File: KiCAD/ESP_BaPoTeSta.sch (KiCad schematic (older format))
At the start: 22 parts, among them P1 Progr, P2 Battery, P3 Power, P4 Upload, P5 Config, U1 MCP1700-330, U2 ESP-12, U3 DS18B20, U4 DHT22

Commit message: ENH: replace 4k7 resistor by 2 10k
so I don't have to buy 4k7 resistors
Enlarge ground plane beneath ESP
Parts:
- added R11: 10k, Resistors_SMD:R_1206_HandSoldering, symbol R
- R7: value 4k7 -> 10k
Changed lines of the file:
@@
 $EndComp
 $Comp
-L VCC #PWR01
+L VCC #PWR4
 U 1 1 566291DB
 P 5850 2100
-F 0 "#PWR01" H 5850 1950 50  0001 C CNN
+F 0 "#PWR4" H 5850 1950 50  0001 C CNN
 F 1 "VCC" H 5850 2250 50  0000 C CNN
 F 2 "" H 5850 2100 50  0000 C CNN
@@
 $EndComp
 $Comp
-L GND #PWR02
+L GND #PWR5
 U 1 1 56629270
 P 5850 3950
-F 0 "#PWR02" H 5850 3700 50  0001 C CNN
+F 0 "#PWR5" H 5850 3700 50  0001 C CNN
 F 1 "GND" H 5850 3800 50  0000 C CNN
 F 2 "" H 5850 3950 50  0000 C CNN
@@
 	6950 2800 6950 1650
 $Comp
-L GND #PWR03
+L GND #PWR6
 U 1 1 5662AF46
 P 7050 1750
-F 0 "#PWR03" H 7050 1500 50  0001 C CNN
+F 0 "#PWR6" H 7050 1500 50  0001 C CNN
 F 1 "GND" H 7050 1600 50  0000 C CNN
 F 2 "" H 7050 1750 50  0000 C CNN
@@
 	4600 2500 2150 2500
 $Comp
-L PWR_FLAG #FLG04
+L PWR_FLAG #FLG1
 U 1 1 5662B03F
 P 1550 2100
-F 0 "#FLG04" H 1550 2195 50  0001 C CNN
+F 0 "#FLG1" H 1550 2195 50  0001 C CNN
 F 1 "PWR_FLAG" H 1550 2280 50  0000 C CNN
 F 2 "" H 1550 2100 50  0000 C CNN
@@
 $EndComp
 $Comp
-L PWR_FLAG #FLG05
+L PWR_FLAG #FLG2
 U 1 1 5662B14A
 P 1550 3000
-F 0 "#FLG05" H 1550 3095 50  0001 C CNN
+F 0 "#FLG2" H 1550 3095 50  0001 C CNN
 F 1 "PWR_FLAG" H 1550 3180 50  0000 C CNN
 F 2 "" H 1550 3000 50  0000 C CNN
@@
 P 4900 1100
 F 0 "R7" V 4980 1100 50  0000 C CNN
-F 1 "4k7" V 4900 1100 50  0000 C CNN
+F 1 "10k" V 4900 1100 50  0000 C CNN
 F 2 "Resistors_SMD:R_1206_HandSoldering" V 4830 1100 50  0001 C CNN
 F 3 "" H 4900 1100 50  0000 C CNN
@@
 $EndComp
 Wire Wire Line
-	4900 1250 5050 1250
+	4750 1250 5050 1250
 $Comp
 L CONN_01X02 P2
@@
 	1550 2600 1550 3000
 $Comp
-L +BATT #PWR06
+L +BATT #PWR1
 U 1 1 5662D0E0
 P 1550 2100
-F 0 "#PWR06" H 1550 1950 50  0001 C CNN
+F 0 "#PWR1" H 1550 1950 50  0001 C CNN
 F 1 "+BATT" H 1550 2240 50  0000 C CNN
 F 2 "" H 1550 2100 50  0000 C CNN
@@
 PwrSens
 Wire Wire Line
-	4900 950  5050 950
+	4750 950  5050 950
 Wire Wire Line
 	5050 950  5050 1150
@@
 	3000 3900 7600 3900
 $Comp
-L GND #PWR07
+L GND #PWR3
 U 1 1 568F994B
 P 5050 1550
-F 0 "#PWR07" H 5050 1300 50  0001 C CNN
+F 0 "#PWR3" H 5050 1300 50  0001 C CNN
 F 1 "GND" H 5050 1400 50  0000 C CNN
 F 2 "" H 5050 1550 50  0000 C CNN
@@
 	5050 1550 5050 1350
 $Comp
-L GND #PWR08
+L GND #PWR2
 U 1 1 568F99FF
 P 4100 1550
-F 0 "#PWR08" H 4100 1300 50  0001 C CNN
+F 0 "#PWR2" H 4100 1300 50  0001 C CNN
 F 1 "GND" H 4100 1400 50  0000 C CNN
 F 2 "" H 4100 1550 50  0000 C CNN
@@
 Connection ~ 3800 3900
 Connection ~ 3800 2100
+$Comp
+L R R11
+U 1 1 5692C067
+P 4750 1100
+F 0 "R11" V 4830 1100 50  0000 C CNN
+F 1 "10k" V 4750 1100 50  0000 C CNN
+F 2 "Resistors_SMD:R_1206_HandSoldering" V 4680 1100 50  0001 C CNN
+F 3 "" H 4750 1100 50  0000 C CNN
+	1    4750 1100
+	1    0    0    -1
+$EndComp
+Connection ~ 4900 1250
+Connection ~ 4900 950
 $EndSCHEMATC

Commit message: ENH: improve battery measurement accuracy
use 56k instead of 68k resistor
This will work up to 6.6V -- more than enough, as max
rated input voltage of the MCP1700 is only 6V
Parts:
- R1: value 68k -> 56k
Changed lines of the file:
@@
 $EndComp
 $Comp
-L VCC #PWR4
+L VCC #PWR01
 U 1 1 566291DB
 P 5850 2100
-F 0 "#PWR4" H 5850 1950 50  0001 C CNN
+F 0 "#PWR01" H 5850 1950 50  0001 C CNN
 F 1 "VCC" H 5850 2250 50  0000 C CNN
 F 2 "" H 5850 2100 50  0000 C CNN
@@
 $EndComp
 $Comp
-L GND #PWR5
+L GND #PWR02
 U 1 1 56629270
 P 5850 3950
-F 0 "#PWR5" H 5850 3700 50  0001 C CNN
+F 0 "#PWR02" H 5850 3700 50  0001 C CNN
 F 1 "GND" H 5850 3800 50  0000 C CNN
 F 2 "" H 5850 3950 50  0000 C CNN
@@
 P 2150 2250
 F 0 "R1" V 2230 2250 50  0000 C CNN
-F 1 "68k" V 2150 2250 50  0000 C CNN
+F 1 "56k" V 2150 2250 50  0000 C CNN
 F 2 "Resistors_SMD:R_1206_HandSoldering" V 2080 2250 50  0001 C CNN
 F 3 "" H 2150 2250 50  0000 C CNN
@@
 	6950 2800 6950 1650
 $Comp
-L GND #PWR6
+L GND #PWR03
 U 1 1 5662AF46
 P 7050 1750
-F 0 "#PWR6" H 7050 1500 50  0001 C CNN
+F 0 "#PWR03" H 7050 1500 50  0001 C CNN
 F 1 "GND" H 7050 1600 50  0000 C CNN
 F 2 "" H 7050 1750 50  0000 C CNN
@@
 	4600 2500 2150 2500
 $Comp
-L PWR_FLAG #FLG1
+L PWR_FLAG #FLG04
 U 1 1 5662B03F
 P 1550 2100
-F 0 "#FLG1" H 1550 2195 50  0001 C CNN
+F 0 "#FLG04" H 1550 2195 50  0001 C CNN
 F 1 "PWR_FLAG" H 1550 2280 50  0000 C CNN
 F 2 "" H 1550 2100 50  0000 C CNN
@@
 $EndComp
 $Comp
-L PWR_FLAG #FLG2
+L PWR_FLAG #FLG05
 U 1 1 5662B14A
 P 1550 3000
-F 0 "#FLG2" H 1550 3095 50  0001 C CNN
+F 0 "#FLG05" H 1550 3095 50  0001 C CNN
 F 1 "PWR_FLAG" H 1550 3180 50  0000 C CNN
 F 2 "" H 1550 3000 50  0000 C CNN
@@
 	1550 2600 1550 3000
 $Comp
-L +BATT #PWR1
+L +BATT #PWR06
 U 1 1 5662D0E0
 P 1550 2100
-F 0 "#PWR1" H 1550 1950 50  0001 C CNN
+F 0 "#PWR06" H 1550 1950 50  0001 C CNN
 F 1 "+BATT" H 1550 2240 50  0000 C CNN
 F 2 "" H 1550 2100 50  0000 C CNN
@@
 	3000 3900 7600 3900
 $Comp
-L GND #PWR3
+L GND #PWR07
 U 1 1 568F994B
 P 5050 1550
-F 0 "#PWR3" H 5050 1300 50  0001 C CNN
+F 0 "#PWR07" H 5050 1300 50  0001 C CNN
 F 1 "GND" H 5050 1400 50  0000 C CNN
 F 2 "" H 5050 1550 50  0000 C CNN
@@
 	5050 1550 5050 1350
 $Comp
-L GND #PWR2
+L GND #PWR08
 U 1 1 568F99FF
 P 4100 1550
-F 0 "#PWR2" H 4100 1300 50  0001 C CNN
+F 0 "#PWR08" H 4100 1300 50  0001 C CNN
 F 1 "GND" H 4100 1400 50  0000 C CNN
 F 2 "" H 4100 1550 50  0000 C CNN

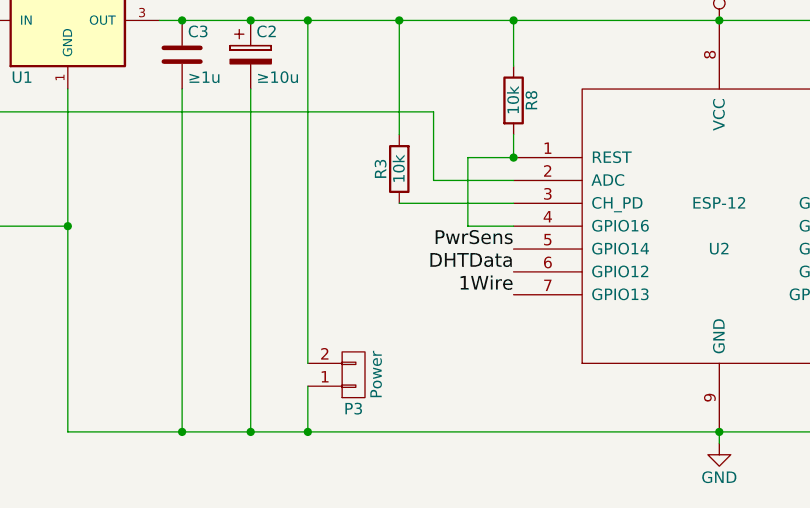
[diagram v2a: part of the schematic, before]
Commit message: ENH: [pcb] add SMD jumpers for data lines
makes it easier to re-use unused lines as GPIO
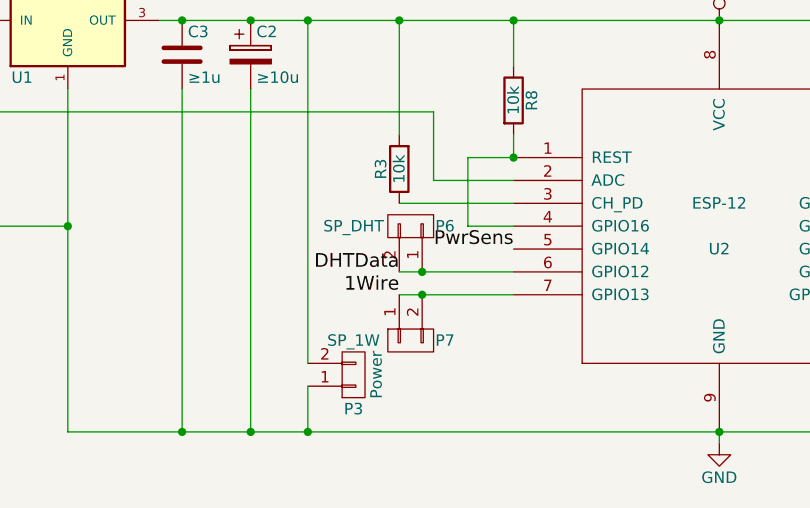
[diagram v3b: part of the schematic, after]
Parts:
- added P6: SP_DHT, open-project:S_JUMPER_2, symbol CONN_01X02
- added P7: SP_1W, open-project:S_JUMPER_2, symbol CONN_01X02
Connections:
- wire segments 48 -> 50
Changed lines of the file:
@@
 LIBS:maxim
 LIBS:sensors
+LIBS:open-project
 LIBS:ESP_BaPoTeSta-cache
 EELAYER 25 0
@@
 	1    0    0    -1
 $EndComp
-Text Label 4950 3300 2    60   ~ 0
+Text Label 4450 3300 2    60   ~ 0
 1Wire
 Text Label 4950 1250 3    60   ~ 0
@@
 	-1   0    0    -1
 $EndComp
-Text Label 4950 3200 2    60   ~ 0
+Text Label 4450 3200 2    60   ~ 0
 DHTData
 Text Label 3650 1250 3    60   ~ 0
@@
 Connection ~ 4900 1250
 Connection ~ 4900 950
+$Comp
+L CONN_01X02 P6
+U 1 1 569544C5
+P 4500 3000
+F 0 "P6" V 4500 3150 50  0000 C CNN
+F 1 "SP_DHT" V 4500 2750 50  0000 C CNN
+F 2 "open-project:S_JUMPER_2" H 4500 3000 50  0001 C CNN
+F 3 "" H 4500 3000 50  0000 C CNN
+	1    4500 3000
+	0    1    -1   0
+$EndComp
+$Comp
+L CONN_01X02 P7
+U 1 1 56954571
+P 4500 3500
+F 0 "P7" V 4500 3350 50  0000 C CNN
+F 1 "SP_1W" V 4500 3750 50  0000 C CNN
+F 2 "open-project:S_JUMPER_2" H 4500 3500 50  0001 C CNN
+F 3 "" H 4500 3500 50  0000 C CNN
+	1    4500 3500
+	0    -1   1    0
+$EndComp
+Wire Wire Line
+	4450 3200 4950 3200
+Wire Wire Line
+	4450 3300 4950 3300
+Connection ~ 4550 3200
+Connection ~ 4550 3300
 $EndSCHEMATC

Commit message: ENH: [pcb] minor silkscreen fixes
also, finish f41bc1a
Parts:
- C2: footprint Capacitors_ThroughHole:C_Radial_D5_L11_P2 -> Capacitors_ThroughHole:C_Radial_D5_L11_P2.5
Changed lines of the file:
@@
 F 0 "C2" H 3825 2350 50  0000 L CNN
 F 1 "≥10u" H 3825 2150 50  0000 L CNN
-F 2 "Capacitors_ThroughHole:C_Radial_D5_L11_P2" H 3838 2100 50  0001 C CNN
+F 2 "Capacitors_ThroughHole:C_Radial_D5_L11_P2.5" H 3838 2100 50  0001 C CNN
 F 3 "" H 3800 2250 50  0000 C CNN
 	1    3800 2250

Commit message: ENH: started work on new board layout
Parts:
- removed P6: SP_DHT, open-project:S_JUMPER_2, symbol CONN_01X02
- removed P7: SP_1W, open-project:S_JUMPER_2, symbol CONN_01X02
- removed R10, R11, R7: 10k, Resistors_SMD:R_1206_HandSoldering, symbol R
- removed U2: ESP-12, ESP8266:ESP-12, symbol ESP-12
- removed U3: DS18B20, TO_SOT_Packages_THT:TO-92_Inline_Wide, symbol DS18B20
- removed U4: DHT22, Pin_Headers:Pin_Header_Straight_1x04, symbol DHT11
- added P10, P11, P12: CONN_01X04, symbol CONN_01X04
- added P13, P14, P15: CONN_01X03, symbol CONN_01X03
- added U2: ESP-12E, symbol ESP-12E
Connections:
- net labels added: BattFET, SCL, SDA
- wire segments 50 -> 71
- no-connect marks 1 -> 3
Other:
- moved on the sheet: R6

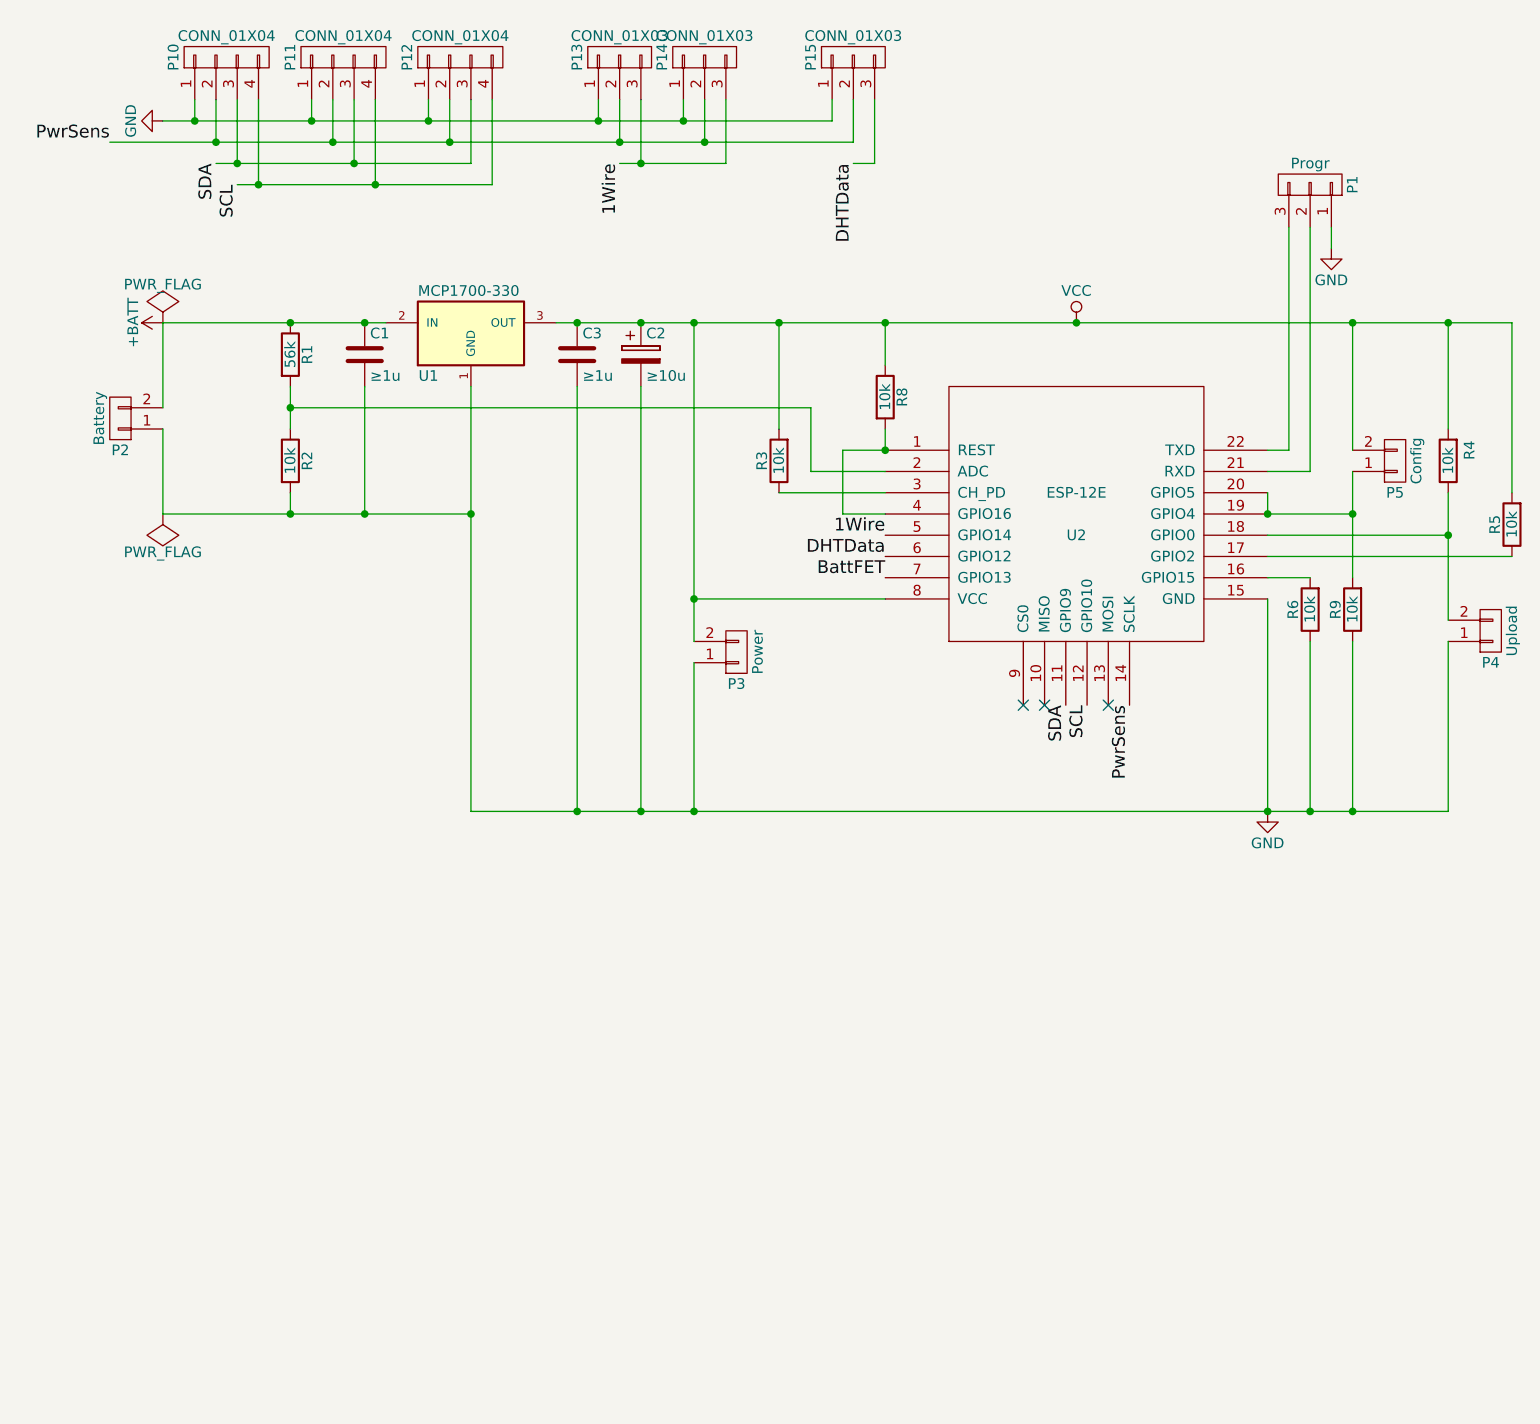
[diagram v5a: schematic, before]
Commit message: ENH: Redesigned schematic
now with 4 I2C, 2 1Wire and 1 DHT port.
Also added MOSFET for battery measurement,
and power-saving Schottky for GPIO16 -- thanks Malte!
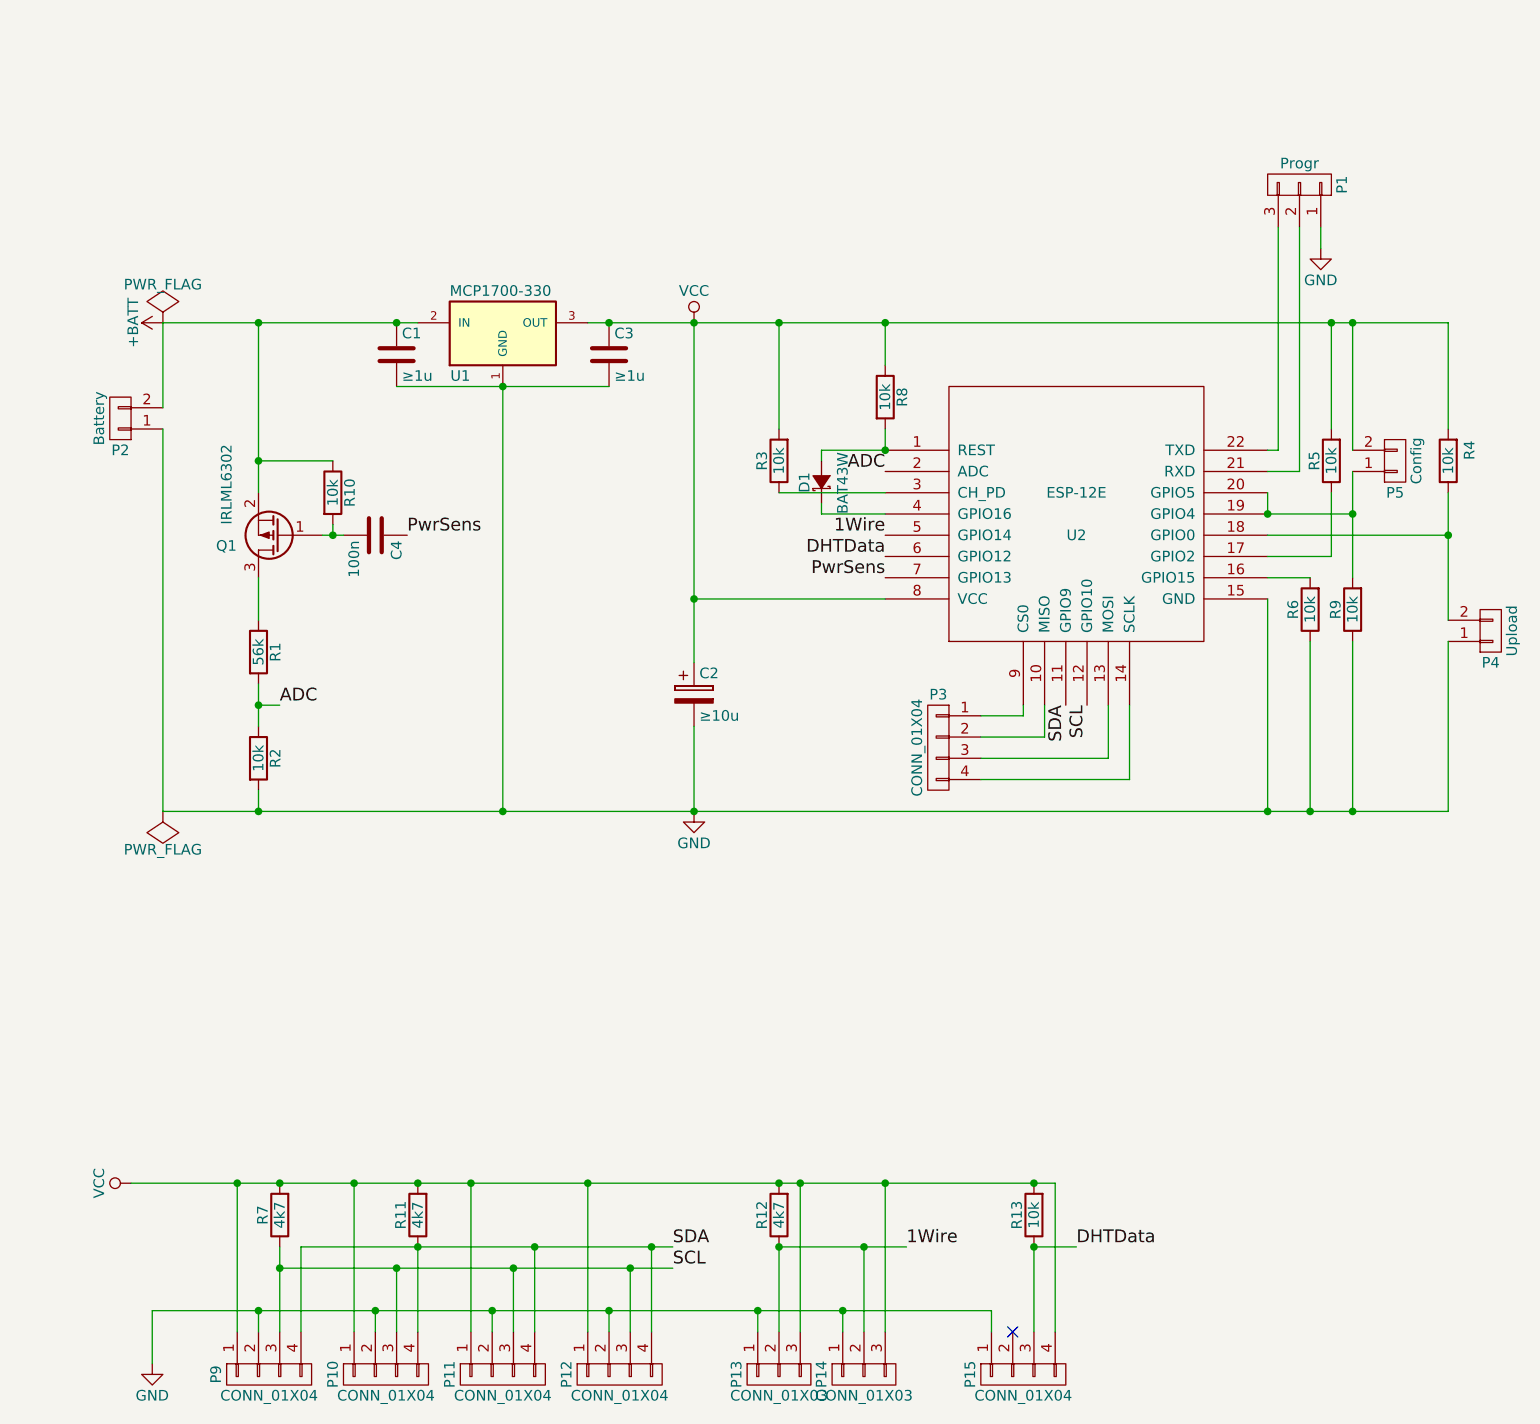
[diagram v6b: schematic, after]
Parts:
- removed P15: CONN_01X03, symbol CONN_01X03
- removed P3: Power, Pin_Headers:Pin_Header_Straight_1x02, symbol CONN_01X02
- added C4: 100n, Capacitors_SMD:C_1206_HandSoldering, symbol C
- added D1: BAT43W, symbol D_Schottky_Small
- added P15, P3, P9: CONN_01X04, symbol CONN_01X04
- added Q1: IRLML6302, symbol Q_PMOS_GSD
- added R10, R13: 10k, Resistors_SMD:R_1206_HandSoldering, symbol R
- added R11, R12, R7: 4k7, Resistors_SMD:R_1206_HandSoldering, symbol R
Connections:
- net BattFET is gone; now on net PwrSens: U2.7 (GPIO13)
- net +BATT: now also Q1.2 (S), R10.1; no longer R1.1
- net 1Wire: now also P13.2 (P2), P14.2 (P2), R12.1; no longer P13.3 (P3), P14.3 (P3)
- net DHTData: now also P15.3 (P3), R13.1
- net GND: now also P10.2 (P2), P11.2 (P2), P12.2 (P2), P15.1 (P1), P9.2 (P2); no longer P10.1 (P1), P11.1 (P1), P12.1 (P1)
- net PwrSens: now also C4.1; no longer P10.2 (P2), P11.2 (P2), P12.2 (P2), P13.2 (P2), P14.2 (P2), U2.14 (SCLK)
- net SCL: now also P10.3 (P3), P11.3 (P3), P12.3 (P3), P9.3 (P3), R7.1; no longer P10.4 (P4), P11.4 (P4), P12.4 (P4)
- net SDA: now also P10.4 (P4), P11.4 (P4), P12.4 (P4), P9.4 (P4), R11.1; no longer P10.3 (P3), P11.3 (P3), P12.3 (P3)
- net VCC: now also P10.1 (P1), P11.1 (P1), P12.1 (P1), P13.3 (P3), P14.3 (P3), P15.4 (P4), P9.1 (P1), R11.2, R12.2, R13.2, R7.2
- net ADC: now reaches R1.2, R2.1, U2.2 (ADC)
- net at R8.2, U2.1 (REST): now also D1.2 (A); no longer U2.4 (GPIO16)
- net at U2.10 (MISO): now also P3.2 (P2)
- net at U2.13 (MOSI): now also P3.3 (P3)
- net at U2.9 (CS0): now also P3.1 (P1)
- new net: Q1.3 (D), R1.1
- new net: P3.4 (P4), U2.14 (SCLK)
- new net: D1.1 (K), U2.4 (GPIO16)
- new net: C4.2, Q1.1 (G), R10.2
- no-connect marks 3 -> 1
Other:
- moved on the sheet: C1, C2, C3, P1, P10, P11, P12, P13, P14, R1, R2, R5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
